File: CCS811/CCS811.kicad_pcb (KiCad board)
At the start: 2 copper layers, 25.4 x 17.8 mm, 30 parts, among them J1 Conn_01x04, J2 Conn_01x04, J3 Conn_01x06, J4 Conn_01x06, Q1 BSS138DW, Q2 BSS138DW, U1 AP2127K-3.3, U2 CCS811

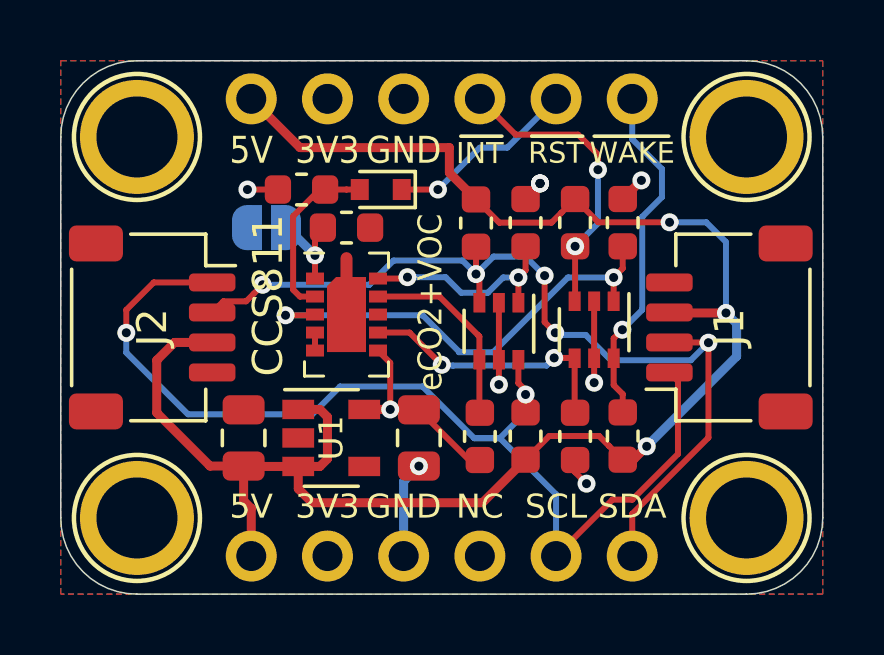
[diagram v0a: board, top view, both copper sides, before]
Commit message: Copper Pour Edits
Copper pour reduced to have 0.2mm edge clearance
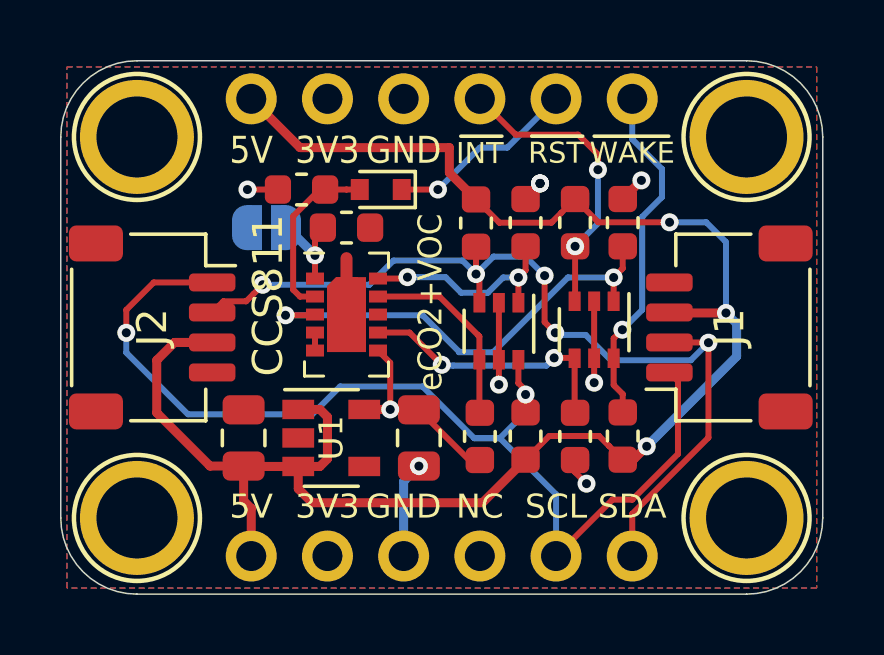
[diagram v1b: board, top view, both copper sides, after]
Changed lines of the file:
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@@
     (polygon
       (pts
-        (xy 52.578 27.0764) (xy 77.978 27.0764) (xy 77.978 44.8564) (xy 52.578 44.8564)
+        (xy 52.7812 27.2796) (xy 77.7748 27.2796) (xy 77.7748 44.6532) (xy 52.7812 44.6532)
       )
     )
@@
     (polygon
       (pts
-        (xy 52.578 27.0764) (xy 77.978 27.0764) (xy 77.978 44.8564) (xy 52.578 44.8564)
+        (xy 52.7812 27.2796) (xy 77.7748 27.2796) (xy 77.7748 44.6532) (xy 52.7812 44.6532)
       )
     )

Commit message: Ground Plane edit
Joint Added
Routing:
- net GND: track 5.24 -> 7.84 mm, vias 1 -> 3
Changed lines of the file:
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@@
     (thickness 1.6)
     (drawings 152)
-    (tracks 218)
+    (tracks 221)
     (zones 0)
     (modules 30)
@@
   )
   (setup
-    (last_trace_width 0.127)
+    (last_trace_width 0.4)
     (user_trace_width 0.2)
     (user_trace_width 0.25)
@@
   (segment (start 64.008 43.5864) (end 64.008 41.0972) (width 0.3) (layer B.Cu) (net 1))
   (segment (start 62.103 35.687) (end 62.103 33.655) (width 0.4) (layer F.Cu) (net 1))
+  (via (at 69.342 30.2895) (size 0.6) (drill 0.3) (layers F.Cu B.Cu) (net 1))
+  (via (at 71.755 29.845) (size 0.6) (drill 0.3) (layers F.Cu B.Cu) (net 1))
+  (segment (start 69.7865 29.845) (end 69.342 30.2895) (width 0.4) (layer B.Cu) (net 1))
+  (segment (start 71.755 29.845) (end 69.7865 29.845) (width 0.4) (layer B.Cu) (net 1))
   (segment (start 58.674 40.5869) (end 58.674 41.7449) (width 0.3) (layer F.Cu) (net 2))
   (segment (start 58.928 41.9989) (end 58.928 43.5864) (width 0.3) (layer F.Cu) (net 2))
@@
   (segment (start 71.3105 38.1889) (end 71.3105 38.7984) (width 0.2) (layer F.Cu) (net 15))
   (segment (start 71.008 37.8864) (end 71.3105 38.1889) (width 0.2) (layer F.Cu) (net 15))
-  (segment (start 71.628 29.6926) (end 71.628 28.3464) (width 0.2) (layer B.Cu) (net 15))
-  (segment (start 72.6186 30.6832) (end 71.628 29.6926) (width 0.2) (layer B.Cu) (net 15))
-  (segment (start 72.6186 31.623) (end 72.6186 30.6832) (width 0.2) (layer B.Cu) (net 15))
+  (segment (start 72.6186 29.337) (end 71.628 28.3464) (width 0.2) (layer B.Cu) (net 15))
+  (segment (start 72.6186 31.623) (end 72.6186 29.337) (width 0.2) (layer B.Cu) (net 15))
   (segment (start 71.9582 32.2834) (end 72.6186 31.623) (width 0.2) (layer B.Cu) (net 15))
   (segment (start 71.2978 36.0426) (end 71.9582 35.3822) (width 0.2) (layer B.Cu) (net 15))

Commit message: Soldermask width adjusted
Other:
- rule solder_mask_min_width: 0.1 -> 0.05
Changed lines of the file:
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@@
   )
   (setup
-    (last_trace_width 0.4)
+    (last_trace_width 0.127)
     (user_trace_width 0.2)
     (user_trace_width 0.25)
@@
     (pad_drill 1)
     (pad_to_mask_clearance 0)
-    (solder_mask_min_width 0.1)
+    (solder_mask_min_width 0.05)
     (aux_axis_origin 0 0)
     (visible_elements 7FFFFFFF)
